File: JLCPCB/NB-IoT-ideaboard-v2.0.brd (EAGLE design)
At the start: 160 x 100 mm, 111 parts, among them Q1 32.768kHz, Q3 9013, Q4 9013, Q5 9013, U1 STM32F103RBT6, U2 MCP73831T-2ACI/OT, U3 AP2112-3.3, U4 PAM2401, U5 MICROSIM, U6 BC92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

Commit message: JLCPCB layout finished
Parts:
- removed C37: 100uF, rcl:C1210
- removed DEBUG: (no value), pinhead:1X03
- removed PWR1: GREEN, led:CHIP-LED0805
- removed S5: DTSM-6, switch-tact:DTSM-6
- removed U8: USBLC6-2SC6YSOT23-6L_STM-L, USBLC6:SOT23-6L_STM-L
- added JP1: (no value), pinhead-2:1X03-S
- added JP2: (no value), pinhead-2:1X05-S
- added LED: GREEN, led:CHIP-LED0805
- added R31: 1k5, rcl:R0805
- added S4: SWITCH-MOMENTARY-2SMD, SparkFun-Electromechanical:TACTILE-SWITCH-SMD
- BOOT: device pinhead-2:2X03SMD -> pinhead-2:2X03
- C10, C11: value 20pF -> 30pF
- C12, C13: value 4p3 -> 15pF
- C15: value 10uF -> 1uF
- C19: value 100nF -> 100uF; device rcl:C0805 -> rcl:B/3528-21R
- C23: device Adafruit111:_0805 -> rcl:C0805
- CC1101, MODEMCTL: device pinhead-2:2X05SMD -> pinhead-2:2X05
- L1: value 39nH -> 33nH; device wuerth-elektronik:0805 -> wuerth-elektronik:0603
- LIPO: value (none) -> C265329
- NET: device led:CHIPLED_0805 -> led:CHIP-LED0805
- R6: value 5k76 -> 5k6
- S2, S3, S6: value DTSM-6 -> SWITCH-MOMENTARY-2SMD; device switch-tact:DTSM-6 -> SparkFun-Electromechanical:TACTILE-SWITCH-SMD
- moved $H4 772.4 mm to (3.25, 64.0)
- moved SPI1 723.5 mm to (35.6, 65.0)
- moved DIGITAL 704.8 mm to (2.44, 22.6), turned to 270 degrees
- moved I2C1 675.4 mm to (22.3, 2.20), turned to 180 degrees
- moved R23 665.2 mm to (43.3, 41.5), turned to 180 degrees
- moved SWD 660.5 mm to (2.44, 40.4), turned to 90 degrees
- moved ANALOG 647.5 mm to (35.1, 2.17)
- moved USART1 637.7 mm to (22.8, 65.0)
- moved CAN 619.6 mm to (12.6, 65.0)
- moved SPI2 615.1 mm to (50.8, 65.0)
- moved CHG 578.1 mm to (86.8, 15.8), turned to 90 degrees
- moved C33 559.7 mm to (72.7, 47.1)
- moved C32 556.8 mm to (72.7, 50.0)
- moved NET 556.4 mm to (47.3, 18.3), turned to 270 degrees
- moved F1 555.0 mm to (89.6, 25.6)
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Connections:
- net PA11 renamed CAN_RX
- net PA12 renamed CAN_TX
- removed net N$15: F1.2, POWER.VBUS
- removed net N$29: MODEMCTL.8, R5.2
- removed net USB_CONN_D_N: POWER.D-, U8.1
- removed net USB_CONN_D_P: POWER.D+, U8.3
- removed net USB_D_N: U8.6
- new net N$12: MODEMCTL.10, R5.2
- new net PC11: DIGITAL.5, U1.52
- new net PC12: DIGITAL.2, U1.53
- new net PC3: ANALOG.3, U1.11
- new net PC6: JP2.2, U1.37
- new net PC8: JP2.4, U1.39
- new net PC9: JP2.5, U1.40
- new net VIN: F1.2, POWER.VBUS, U$1.PWR2
- net +3V3: now also R31.1; no longer C19.2, USART1.4
- net BC92_PWRKEY: now also S3.3; no longer S5.3, S5.4
- net BC92_RESET: now also C23.2; no longer C23.1, S6.4
- net BC92_TX: now also MODEMCTL.8; no longer MODEMCTL.10
- net DBG_RXD: now also JP1.2; no longer DEBUG.2
- net DBG_TXD: now also JP1.3; no longer DEBUG.3
- net GND: now also C19.-, C23.1, JP1.1, JP2.1, S4.1; no longer C19.1, C23.2, C37.2, DEBUG.1, S2.2, S3.2, S5.1, S5.2, S6.2, U8.2
- net I2C1_SCL: now also I2C1.3; no longer I2C1.2
- net I2C1_SDA: now also I2C1.2; no longer I2C1.3
- net JTDO/SWO: no longer DIGITAL.5
- net N$26: now also LED.C; no longer PWR1.C
- net NRST: now also S2.3; no longer S3.3, S3.4
- net PA2: now also DIGITAL.8; no longer DIGITAL.7
- net PA3: now also DIGITAL.7; no longer DIGITAL.8
- net PA4: no longer ANALOG.4
- net PB0: now also ANALOG.4; no longer ANALOG.3
- net PB12: no longer DIGITAL.2
- net PB13: now also LED.A; no longer PWR1.A
- net PC13: now also S4.3; no longer S2.3, S2.4
- net PC7: now also JP2.3
- net STM_RX: now also MODEMCTL.7; no longer MODEMCTL.9
- net STM_TX: now also MODEMCTL.9; no longer MODEMCTL.7
- net USB_D_P: now also R31.2; no longer U8.4
- net V+: now also C19.+; no longer C37.1
- net VBUS: now also USART1.4; no longer U$1.PWR2, U8.5
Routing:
- net V+: track 0.00 -> 199.3 mm, vias 0 -> 7
- net VBUS: track 0.00 -> 118.7 mm, vias 0 -> 1
- net BOOT0: track 0.00 -> 88.5 mm
- net SIM1_RST: track 0.00 -> 52.7 mm
- net PA4: track 0.00 -> 51.4 mm, vias 0 -> 1
- net BC92_PSM_EINT: track 0.00 -> 51.2 mm, vias 0 -> 2
- net PB13: track 0.00 -> 50.2 mm
- net BC92_TX: track 0.00 -> 49.7 mm
- net SIM1_VDD: track 0.00 -> 49.5 mm, vias 0 -> 2
- net NRST: track 0.00 -> 49.3 mm, vias 0 -> 2
- net PA6: track 0.00 -> 48.5 mm, vias 0 -> 2
- net +3V3: track 0.00 -> 44.1 mm, vias 0 -> 15
- net SIM1_DATA: track 0.00 -> 43.8 mm
- net PA7: track 0.00 -> 43.8 mm, vias 0 -> 2
- net I2C1_SCL: track 0.00 -> 43.2 mm
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- added copper zone on layer 1, net +3V3
- added copper zone on layer 15, net +3V3
- added copper zone on layer 1, net GND
- added copper zone on layer 16, net GND
- added copper zone on layer 2, net GND
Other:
- board size 160 x 100 mm -> 99.6 x 67.5 mm

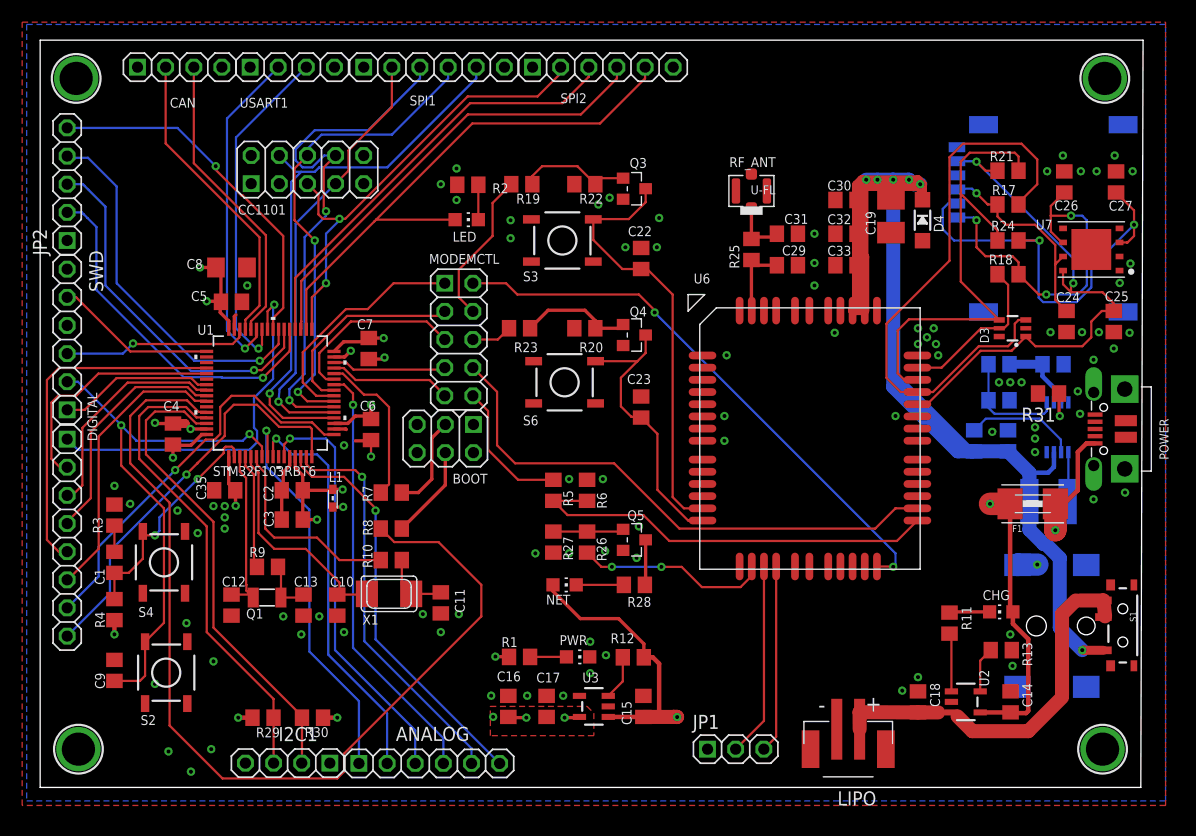
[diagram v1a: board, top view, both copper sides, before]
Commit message: JLCPCB layout tweaks
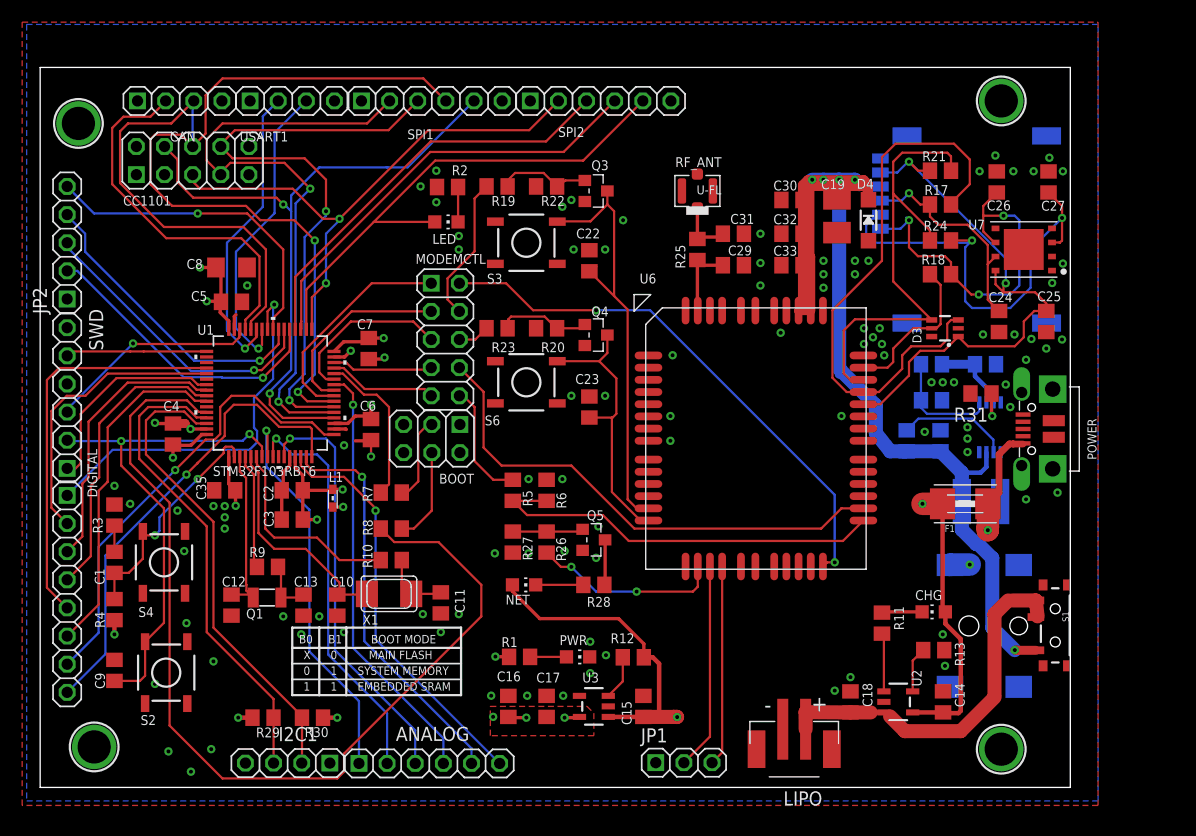
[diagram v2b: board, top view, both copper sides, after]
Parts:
- moved CC1101 10.4 mm to (13.8, 56.6)
- moved $H1 9.57 mm to (86.8, 62.0)
- moved $H3 9.14 mm to (86.8, 3.45)
- moved U5 6.98 mm to (76.7, 58.0)
- moved POWER 6.50 mm to (89.5, 32.4)
- moved C14 6.10 mm to (81.5, 7.73)
- moved C18 6.10 mm to (73.2, 7.72)
- moved C20 6.10 mm to (81.3, 31.3)
- moved C21 6.10 mm to (85.3, 38.2)
- moved C24 6.10 mm to (86.6, 42.1)
- moved C25 6.10 mm to (90.8, 42.1)
- moved C26 6.10 mm to (86.4, 54.7)
- moved CHG 6.10 mm to (80.7, 15.8)
- moved F1 6.10 mm to (83.5, 25.6)
- moved L2 6.10 mm to (84.9, 25.8)
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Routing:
- net V+: track 199.3 -> 165.7 mm, vias 7 -> 6
- net PA7: track 43.8 -> 76.1 mm
- net PA5: track 39.8 -> 57.1 mm, vias 1 -> 2
- net VBUS: track 118.7 -> 102.6 mm
- net PA4: track 51.4 -> 61.1 mm, vias 1 -> 2
- net CAN_RX: track 27.0 -> 36.0 mm
- net PB12: track 42.2 -> 50.4 mm
- net PA6: track 48.5 -> 55.9 mm
- net PC8: track 34.0 -> 27.6 mm
- net CAN_TX: track 27.8 -> 34.2 mm
- net PC7: track 33.3 -> 27.2 mm
- net PC6: track 32.6 -> 27.1 mm
- net PB5: track 21.6 -> 26.7 mm
- net PA3: track 36.5 -> 41.6 mm
- net PA2: track 37.6 -> 42.7 mm
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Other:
- board size 99.6 x 67.5 mm -> 93 x 65 mm
- board text added: "0"
- board text added: "1"
- board text added: "B0"
- board text added: "B1"
- board text added: "BOOT MODE"
- board text added: "EMBEDDED SRAM"
- board text added: "MAIN FLASH"
- board text added: "SYSTEM MEMORY"
- board text added: "X"

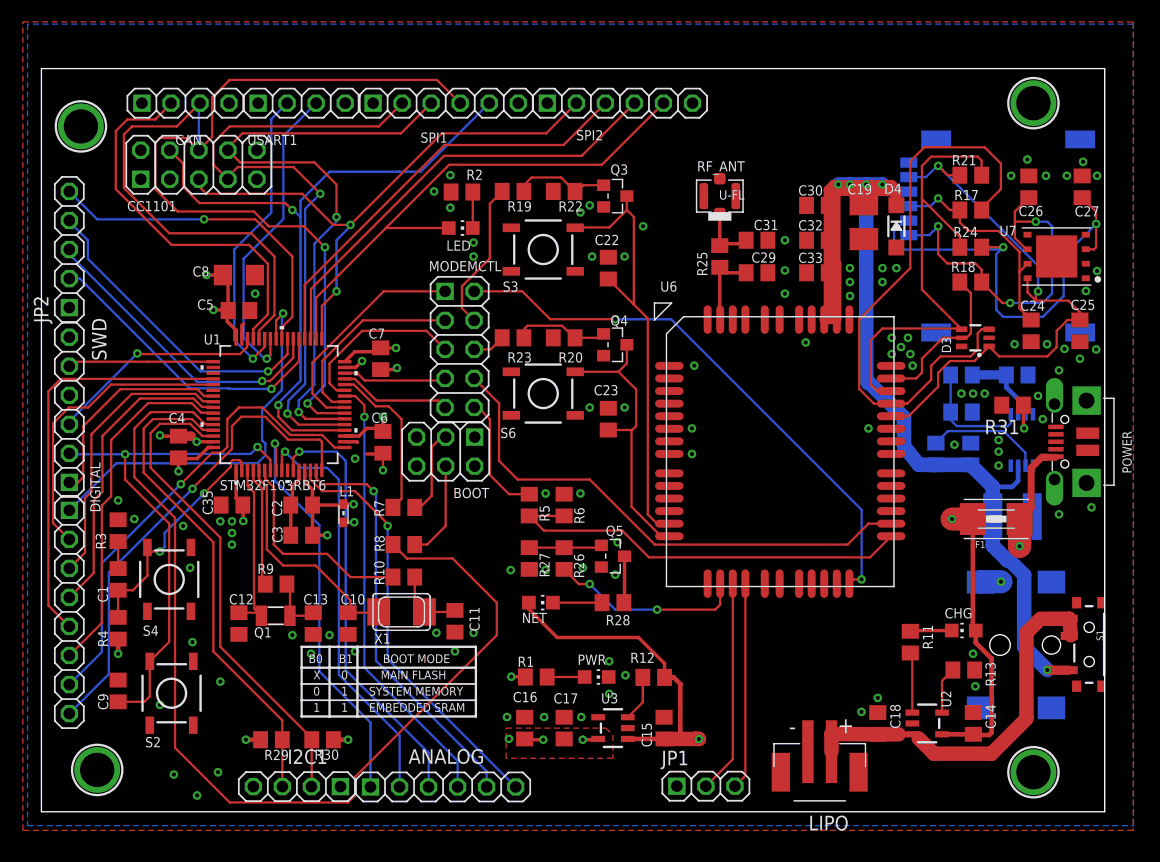
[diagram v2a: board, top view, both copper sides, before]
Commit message: JLCPCB layout SILK EDITS
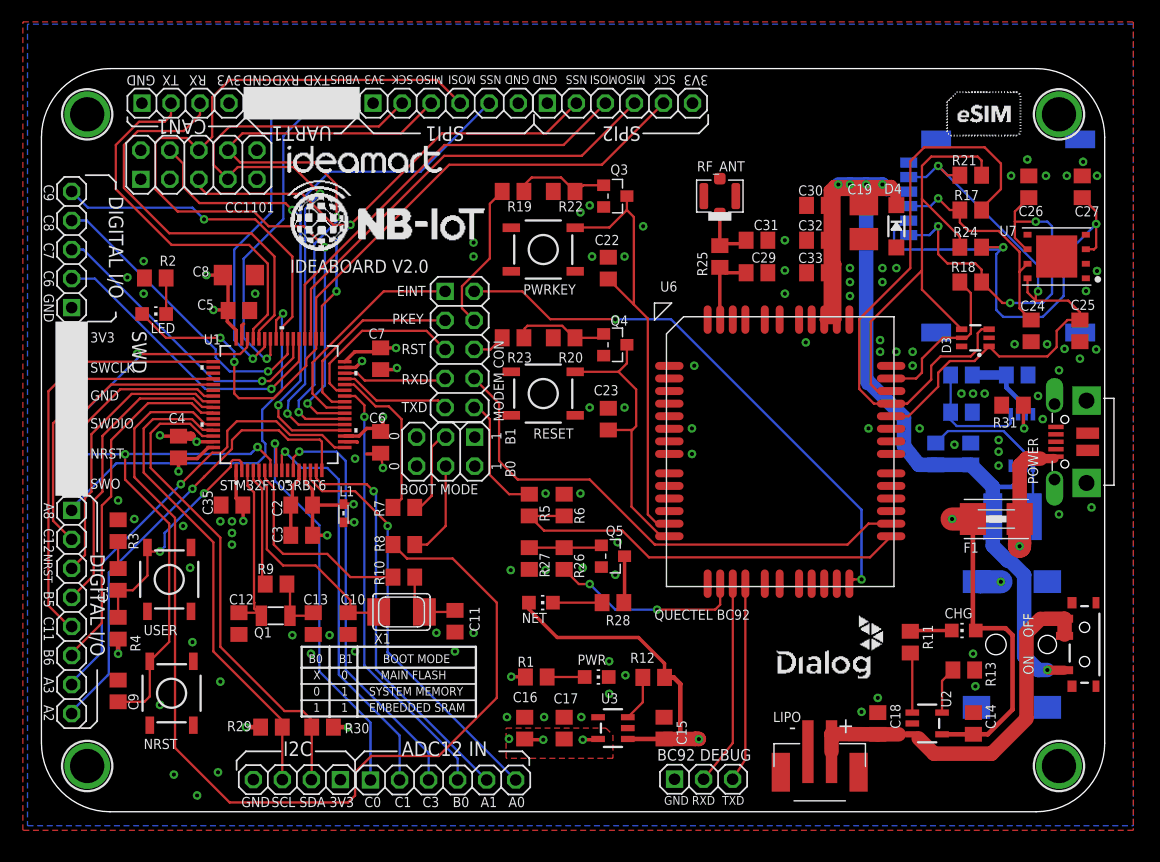
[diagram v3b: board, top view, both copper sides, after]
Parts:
- moved R2 27.9 mm to (9.96, 46.7)
- moved LED 27.9 mm to (9.86, 43.5)
- moved $H1 2.44 mm to (89.0, 61.0)
- moved $H3 2.30 mm to (89.0, 4.00)
- moved $H4 1.19 mm to (4.00, 61.0)
- moved R29 1.10 mm to (20.1, 7.40)
- moved R30 1.10 mm to (24.6, 7.40)
- moved $H2 0.94 mm to (4.00, 4.00)
- moved JP1 0.64 mm to (57.9, 2.84)
- moved ANALOG 0.61 mm to (35.1, 2.78)
- moved I2C1 0.61 mm to (22.3, 2.81)
- moved S1 0.41 mm to (91.2, 14.6)
- moved U$1 0.36 mm to (88.0, 14.6)
- moved DIGITAL 0.20 mm to (2.64, 17.5)
- moved JP2 0.20 mm to (2.64, 49.2)
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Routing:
- net PB13: track 46.5 -> 64.5 mm, vias 0 -> 2
- net PA7: track 76.1 -> 71.6 mm
- net BOOT0: track 88.5 -> 92.0 mm
- net VBUS: track 102.6 -> 105.7 mm
- net PA2: track 42.7 -> 40.9 mm
- net PA3: track 41.6 -> 39.9 mm
- net VIN: track 15.7 -> 16.7 mm
- net DBG_RXD: track 18.7 -> 18.0 mm
- net DBG_TXD: track 18.1 -> 17.4 mm
- net PC3: track 37.8 -> 37.2 mm
- net PC1: track 36.6 -> 35.9 mm
- net PC0: track 36.0 -> 35.3 mm
- net PA1: track 36.2 -> 35.5 mm
- net I2C1_SCL: track 43.2 -> 42.6 mm
- net PC8: track 27.6 -> 27.1 mm
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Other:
- outline, holes or cut-outs redrawn
- board text added: "2020/11/06"
- board text added: "3V3"
- board text added: "9088 4007 7733 3295"
- board text added: "A0"
- board text added: "A1"
- board text added: "A2"
- board text added: "A3"
- board text added: "A8"
- board text added: "ADC12 IN"
- board text added: "B5"
- board text added: "B6"
- board text added: "BC92 DEBUG"
- board text added: "C0"
- board text added: "C1"
- board text added: "C11"
- board text added: "C12"
- board text added: "C3"
- board text added: "C6"
- board text added: "C7"
- board text added: "C8"
- board text added: "C9"
- board text added: "CAN1"
- board text added: "CC1101"
- board text added: "DIGITAL I/O"
- board text added: "EINT"
- board text added: "GND"
- board text added: "I2C"
- board text added: "IDEABOARD V2.0"
- board text added: "INSERT MICRO SIMCARD"
- board text added: "LED"
- board text added: "LIPO"
- board text added: "MISO"
- board text added: "MODEM CON"
- board text added: "MOSI"
- board text added: "NRST"
- board text added: "NSS"
- board text added: "OFF"
- board text added: "ON"
- board text added: "PKEY"
- board text added: "POWER"
- board text added: "PWRKEY"
- board text added: "QUECTEL BC92"
- board text added: "Quectel BC92"
- board text added: "RESET"
- board text added: "RST"
- board text added: "RX"
- board text added: "RXD"
- board text added: "SCK"
- board text added: "SCL"
- board text added: "SDA"
- board text added: "SPI1"
- board text added: "SPI2"
- board text added: "STM32F103RBT6"
- board text added: "SWCLK"
- board text added: "SWD"
- board text added: "SWDIO"
- board text added: "SWO"
- board text added: "TX"
- board text added: "TXD"
- board text added: "UART1"
- board text added: "USER"
- board text added: "VBUS"

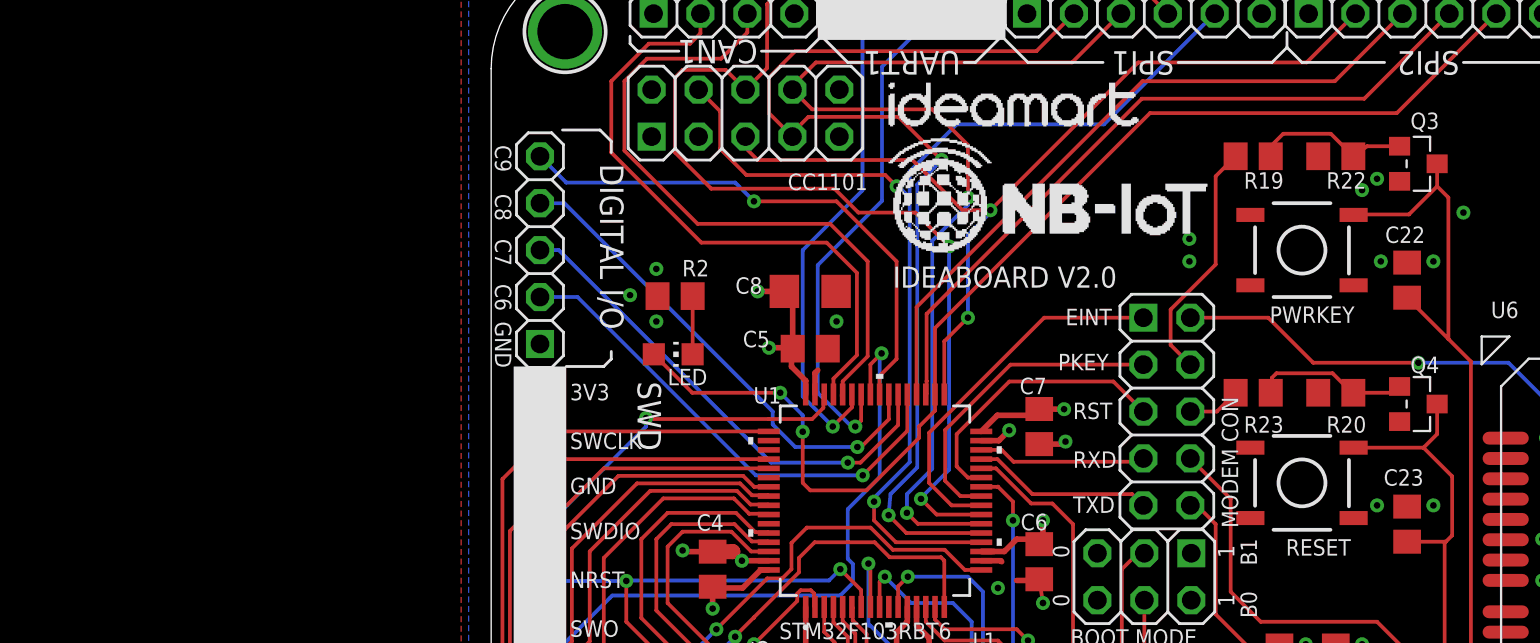
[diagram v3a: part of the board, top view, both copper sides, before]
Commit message: JLCPCB layout SILK EDITS
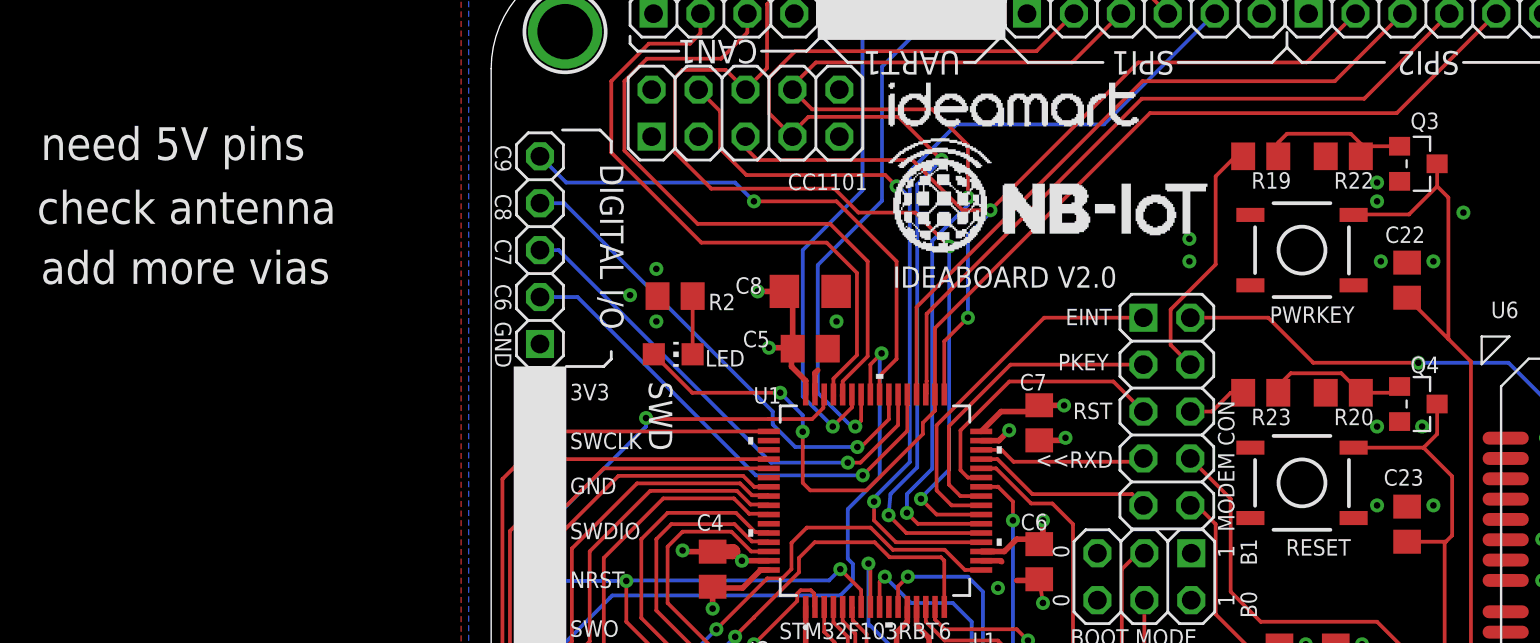
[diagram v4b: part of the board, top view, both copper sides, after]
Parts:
- moved R19 0.41 mm to (41.7, 54.3)
- moved R20 0.41 mm to (46.1, 41.5)
- moved R22 0.41 mm to (46.1, 54.3)
- moved R23 0.41 mm to (41.7, 41.5)
- moved C7 0.20 mm to (29.7, 39.8)
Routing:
- net GND: vias 102 -> 104
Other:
- board text added: "<<RXD"
- board text added: ">>TXD"
- board text added: "add more vias"
- board text added: "check antenna"
- board text added: "need 5V pins"
